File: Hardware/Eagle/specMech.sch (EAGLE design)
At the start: 77 parts, among them J1 PINHD-1X8-MOLEX-SHROUD, J3 PINHD-1X8-MOLEX-SHROUD, J4 PINHD-1X8-MOLEX-SHROUD, J6 Molex 0022232081, J8 Molex 0022232081, U1 MCP23008-E/SO, U10 ADS1115, U11 MCP23008-E/SO, U12 74HC2G17TSSOP-6, U13 ISO7421DR, U14 MB85RC256, U2 MCP23008-E/SO, U3 TXB0102DCURVSSOP8, U4 MCP9808-E/MS, U5 TBD62083, U6 DS3231MZ+, U7 LTC4311ISC6TRPBF, U8 MCP23008-E/SO, U9 ADS1115

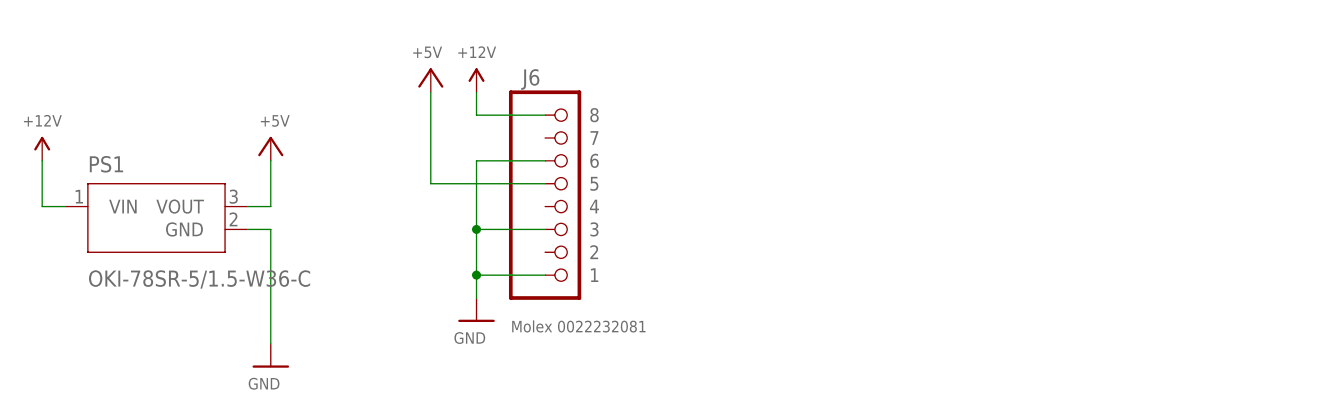
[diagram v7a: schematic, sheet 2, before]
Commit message: Added +5V power for USB isolator (JST 2-pin header)
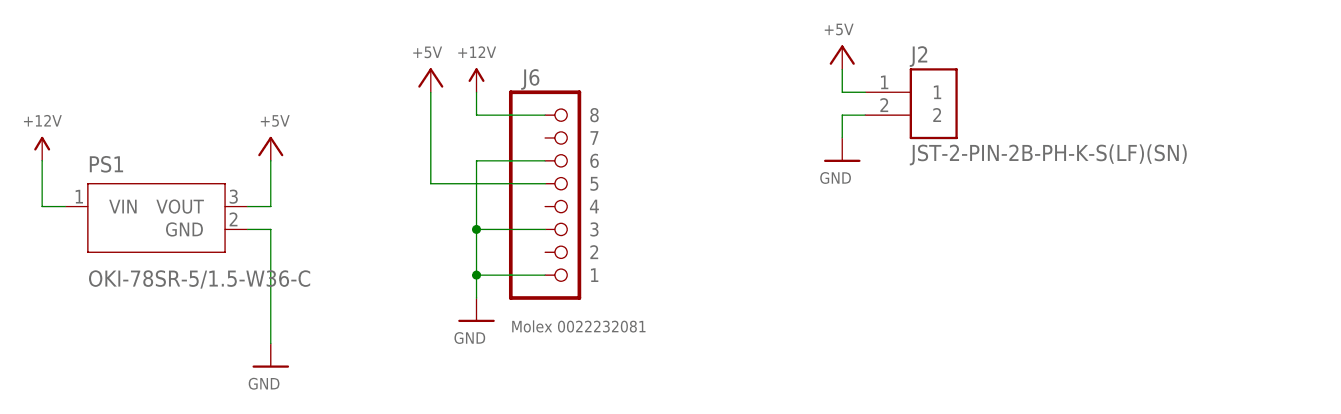
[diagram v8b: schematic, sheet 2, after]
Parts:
- added J2: JST-2-PIN-2B-PH-K-S(LF)(SN), AUmlib:JST-2-PIN-2B-PH-K-S(LF)(SN)
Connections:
- net +5V: now also J2.1
- net GND: now also J2.2
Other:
- note added: "2-pin 2mm header JST B2B-PH-K-S(LF)(SN) DFRobot has connector kits for cables"
- note added: "Power for USB isolator"
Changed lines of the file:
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@@
 <setting verticaltext="up"/>
 </settings>
-<grid distance="0.1" unitdist="inch" unit="inch" style="lines" multiple="1" display="no" altdistance="0.01" altunitdist="inch" altunit="inch"/>
+<grid distance="0.1" unitdist="inch" unit="inch" style="lines" multiple="1" display="yes" altdistance="0.01" altunitdist="inch" altunit="inch"/>
 <layers>
 <layer number="1" name="Top" color="4" fill="1" visible="no" active="no"/>
@@
 <part name="GND45" library="AUmlib" library_urn="urn:adsk.eagle:library:9166017" deviceset="GND" device=""/>
 <part name="J7" library="AUmlib" library_urn="urn:adsk.eagle:library:9166017" deviceset="XPORT" device="XPORT-2" package3d_urn="urn:adsk.eagle:package:18328251/5"/>
+<part name="J2" library="AUmlib" library_urn="urn:adsk.eagle:library:9166017" deviceset="JST-2-PIN-2B-PH-K-S(LF)(SN)" device="" package3d_urn="urn:adsk.eagle:package:24616272/2"/>
+<part name="GND4" library="AUmlib" library_urn="urn:adsk.eagle:library:9166017" deviceset="GND" device=""/>
+<part name="P+27" library="AUmlib" library_urn="urn:adsk.eagle:library:9166017" deviceset="+5V" device=""/>
 </parts>
 <sheets>
@@
 <wire x1="68.58" y1="144.78" x2="68.58" y2="160.02" width="0.254" layer="250"/>
 <text x="177.8" y="27.94" size="2.54" layer="250">+5V Power Supply</text>
+<text x="160.02" y="114.3" size="1.778" layer="250">2-pin 2mm header JST B2B-PH-K-S(LF)(SN)
+DFRobot has connector kits for cables</text>
+<wire x1="154.94" y1="160.02" x2="213.36" y2="160.02" width="0.254" layer="250"/>
+<wire x1="213.36" y1="160.02" x2="213.36" y2="101.6" width="0.254" layer="250"/>
+<wire x1="213.36" y1="101.6" x2="154.94" y2="101.6" width="0.254" layer="250"/>
+<wire x1="154.94" y1="101.6" x2="154.94" y2="160.02" width="0.254" layer="250"/>
+<text x="175.26" y="154.94" size="2.54" layer="250">Power for USB isolator</text>
 </plain>
 <instances>
@@
 <attribute name="NAME" x="83.82" y="128.27" size="1.778" layer="95"/>
 <attribute name="VALUE" x="83.82" y="115.57" size="1.778" layer="96"/>
+</instance>
+<instance part="J2" gate="G$1" x="177.8" y="137.16" smashed="yes">
+<attribute name="NAME" x="175.255640625" y="140.46766875" size="1.78105" layer="95"/>
+<attribute name="VALUE" x="175.255409375" y="129.526240625" size="1.781209375" layer="96"/>
+</instance>
+<instance part="GND4" gate="1" x="167.64" y="129.54" smashed="yes">
+<attribute name="VALUE" x="165.1" y="127" size="1.27" layer="96"/>
+</instance>
+<instance part="P+27" gate="1" x="167.64" y="142.24" smashed="yes">
+<attribute name="VALUE" x="168.91" y="144.78" size="1.27" layer="96" rot="R180"/>
 </instance>
 </instances>
@@
 <junction x="127" y="121.92"/>
 </segment>
+<segment>
+<pinref part="GND4" gate="1" pin="GND"/>
+<wire x1="167.64" y1="132.08" x2="167.64" y2="134.62" width="0.1524" layer="91"/>
+<pinref part="J2" gate="G$1" pin="2"/>
+<wire x1="167.64" y1="134.62" x2="170.18" y2="134.62" width="0.1524" layer="91"/>
+</segment>
 </net>
 <net name="+5V" class="0">
@@
 <wire x1="121.92" y1="127" x2="121.92" y2="137.16" width="0.1524" layer="91"/>
 </segment>
-</net>
+<segment>
+<pinref part="J2" gate="G$1" pin="1"/>
+<wire x1="170.18" y1="137.16" x2="167.64" y2="137.16" width="0.1524" layer="91"/>
+<pinref part="P+27" gate="1" pin="+5V"/>
+<wire x1="167.64" y1="137.16" x2="167.64" y2="139.7" width="0.1524" layer="91"/>
+</segment>
+</net>
